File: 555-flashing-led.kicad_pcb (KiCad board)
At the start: 2 copper layers, 66.8 x 98.6 mm, 9 parts, among them U1 7555

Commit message: finalize pcb
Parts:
- R3, R4: value 1k -> 100
- moved R4 53.5 mm to (114.0, 110.0)
- moved R1 34.6 mm to (114.0, 86.3), turned to 0 degrees
- moved D1 30.3 mm to (84.1, 55.6)
- moved C1 30.2 mm to (104.4, 107.2), turned to 180 degrees
- moved R2 27.8 mm to (114.0, 94.2), turned to 0 degrees
- moved R3 26.6 mm to (114.0, 102.1)
- moved D2 26.3 mm to (109.6, 55.6)
- moved U1 12.2 mm to (101.9, 97.9), turned to 90 degrees
- moved BT1 2.15 mm to (95.4, 98.3)
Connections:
- BT1 pad 1: GNDREF -> +3V0
- BT1 pad 2: +3V0 -> GNDREF
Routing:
- net GNDREF: track 0.00 -> 119.7 mm
- net Net-(D2-A): track 0.00 -> 75.4 mm
- net Net-(D1-A): track 0.00 -> 64.8 mm
- net Net-(U1-THRESHOLD): track 0.00 -> 58.8 mm
- net +3V0: track 0.00 -> 48.1 mm
- net Net-(U1-OUTPUT): track 0.00 -> 19.1 mm
- net Net-(U1-DISCHARGE): track 0.00 -> 19.1 mm
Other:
- board size 66.8 x 98.6 mm -> 66.8 x 85.3 mm

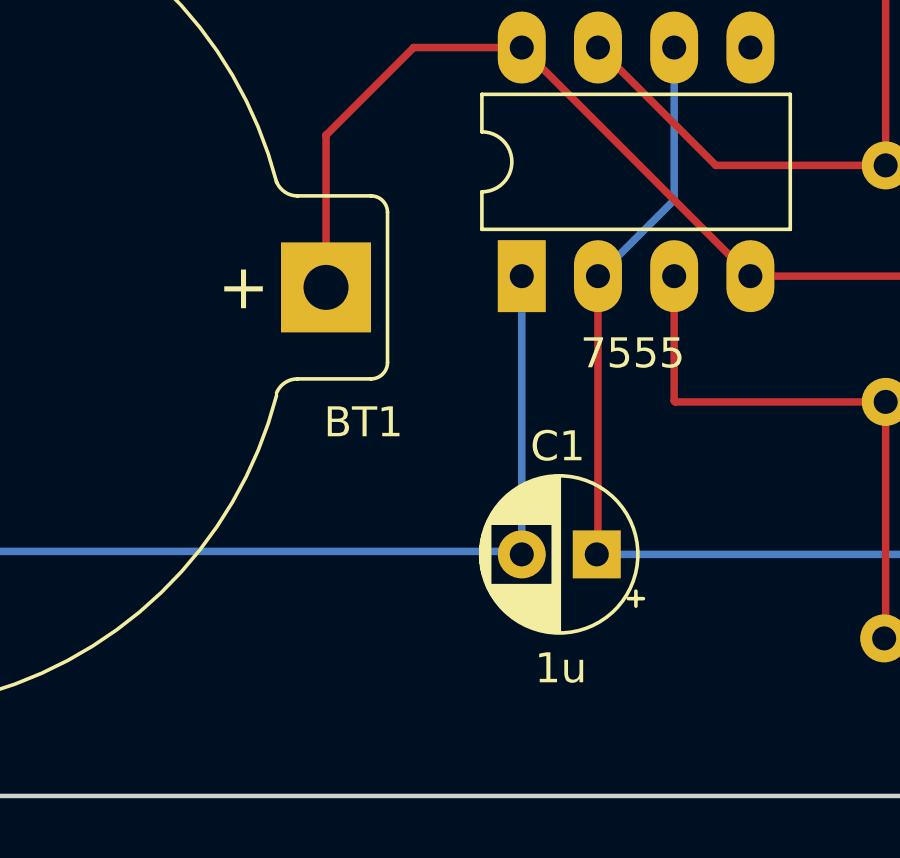
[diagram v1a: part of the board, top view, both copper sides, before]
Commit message: update capacitors
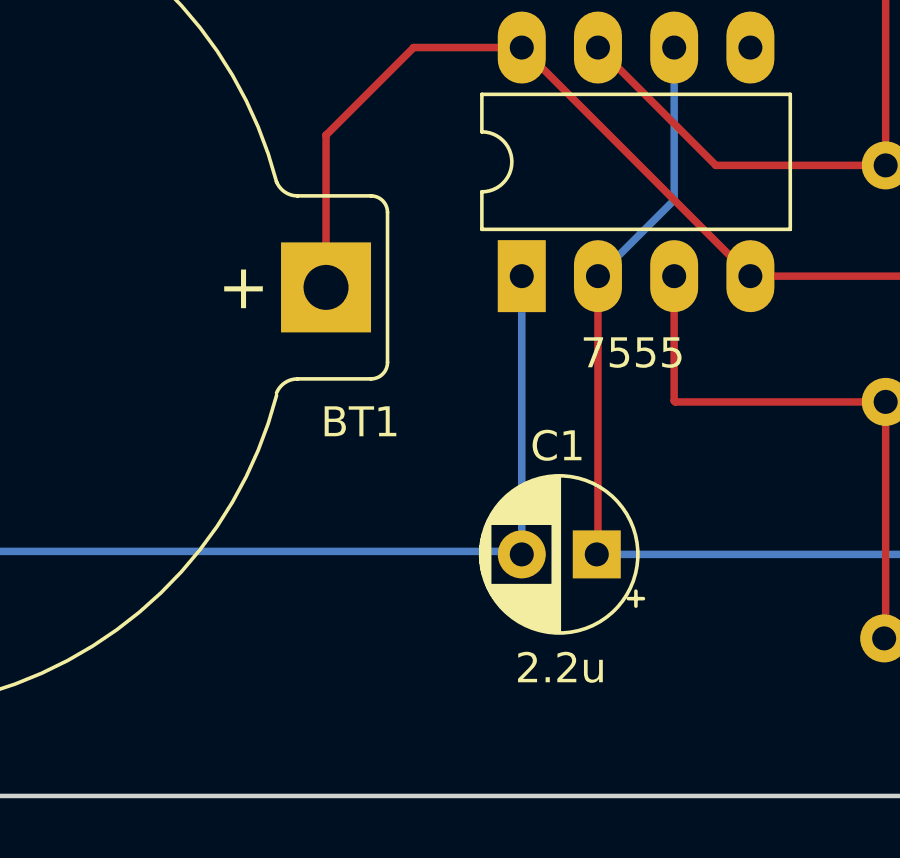
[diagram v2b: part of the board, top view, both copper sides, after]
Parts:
- C1: value 1u -> 2.2u
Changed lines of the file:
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@@
     (property "ki_keywords" "battery cell")
     (attr through_hole)
-    (fp_text reference "BT1" (at -1.25 -4.5) (layer "F.SilkS")
+    (fp_text reference "BT1" (at -1.144999 -4.5) (layer "F.SilkS")
         (effects (font (size 1 1) (thickness 0.15)))
     )
@@
     (fp_arc (start -1.5 3.05) (mid -1.888909 2.888909) (end -2.05 2.5)
       (stroke (width 0.12) (type solid)) (layer "F.SilkS"))
-    (fp_arc (start 0.95 3.05) (mid 1.371573 3.1784) (end 1.65 3.52)
+    (fp_arc (start 0.95 3.05) (mid 1.371575 3.178399) (end 1.65 3.52)
       (stroke (width 0.12) (type solid)) (layer "F.SilkS"))
     (fp_arc (start 1.65 -3.604769) (mid 17.016593 -13.966381) (end 29.2 0)
@@
     (fp_arc (start -1.5 3.3) (mid -2.065685 3.065685) (end -2.3 2.5)
       (stroke (width 0.05) (type solid)) (layer "F.CrtYd"))
-    (fp_arc (start 0.95 3.3) (mid 1.22459 3.381628) (end 1.41 3.6)
+    (fp_arc (start 0.95 3.3) (mid 1.224591 3.381627) (end 1.41 3.6)
       (stroke (width 0.05) (type solid)) (layer "F.CrtYd"))
     (fp_arc (start 1.41 -3.6) (mid 1.224592 -3.381625) (end 0.95 -3.3)
@@
         (effects (font (size 1 1) (thickness 0.15)))
     )
-    (fp_text value "1u" (at 1.2 -3.8) (layer "F.SilkS")
-        (effects (font (size 1 1) (thickness 0.15)))
-    )
+    (fp_text value "2.2u" (at 1.2 -3.8) (layer "F.SilkS")
+        (effects (font (size 1 1) (thickness 0.15)))
+    )
